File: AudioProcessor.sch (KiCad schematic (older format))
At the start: 57 parts, among them J601 Conn_01x03_Female, J602 Conn_02x01, J603 Conn_02x06_Odd_Even, Q501 2N7002, U502 BK8000L, U503 TDA7719, U504 AP2553AW6-7, U505 JW5026

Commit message: Bauteilwerte verändert
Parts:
- R513, R520, R521: value 10K -> 100K
- R514: value 100R -> 1K
- R523, R524: value 47R -> 100R
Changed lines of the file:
@@
 P 1150 6050
 F 0 "R513" H 1000 6000 50  0000 C CNN
-F 1 "10K" H 950 6100 50  0000 C CNN
+F 1 "100K" H 950 6100 50  0000 C CNN
 F 2 "Resistor_SMD:R_0603_1608Metric_Pad1.05x0.95mm_HandSolder" H 1150 6050 50  0001 C CNN
 F 3 "~" H 1150 6050 50  0001 C CNN
@@
 P 1550 5950
 F 0 "R514" V 1450 5800 50  0000 C CNN
-F 1 "100R" V 1450 6100 50  0000 C CNN
+F 1 "1K" V 1450 6100 50  0000 C CNN
 F 2 "Resistor_SMD:R_0603_1608Metric_Pad1.05x0.95mm_HandSolder" H 1550 5950 50  0001 C CNN
 F 3 "~" H 1550 5950 50  0001 C CNN
@@
 P 7450 3050
 F 0 "R523" V 7350 2900 50  0000 C CNN
-F 1 "47R" V 7350 3200 50  0000 C CNN
+F 1 "100R" V 7350 3200 50  0000 C CNN
 F 2 "Resistor_SMD:R_0603_1608Metric_Pad1.05x0.95mm_HandSolder" H 7450 3050 50  0001 C CNN
 F 3 "~" H 7450 3050 50  0001 C CNN
@@
 P 7450 3200
 F 0 "R524" V 7350 3050 50  0000 C CNN
-F 1 "47R" V 7350 3350 50  0000 C CNN
+F 1 "100R" V 7350 3350 50  0000 C CNN
 F 2 "Resistor_SMD:R_0603_1608Metric_Pad1.05x0.95mm_HandSolder" H 7450 3200 50  0001 C CNN
 F 3 "~" H 7450 3200 50  0001 C CNN
@@
 P 2300 4400
 F 0 "R521" V 2500 4400 50  0000 C CNN
-F 1 "10K" V 2400 4400 50  0000 C CNN
+F 1 "100K" V 2400 4400 50  0000 C CNN
 F 2 "Resistor_SMD:R_0603_1608Metric_Pad1.05x0.95mm_HandSolder" H 2300 4400 50  0001 C CNN
 F 3 "~" H 2300 4400 50  0001 C CNN
@@
 P 1300 4200
 F 0 "R520" H 1150 4250 50  0000 C CNN
-F 1 "10K" H 1150 4150 50  0000 C CNN
+F 1 "100K" H 1150 4150 50  0000 C CNN
 F 2 "Resistor_SMD:R_0603_1608Metric_Pad1.05x0.95mm_HandSolder" H 1300 4200 50  0001 C CNN
 F 3 "~" H 1300 4200 50  0001 C CNN

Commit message: Bereit zur Bestellung
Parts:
- removed C509, C536: 10u, Capacitor_THT:CP_Radial_D4.0mm_P2.00mm, symbol Device:CP1_Small
- removed TP502: TestPoint, TestPoint:TestPoint_Pad_1.0x1.0mm, symbol Connector:TestPoint
- added C509, C536: 10u, Capacitor_SMD:C_1206_3216Metric_Pad1.42x1.75mm_HandSolder, symbol Device:C_Small
- added R20: DNP, Resistor_SMD:R_0603_1608Metric_Pad1.05x0.95mm_HandSolder, symbol Device:R_Small
- C503, C508, C542: footprint Capacitor_THT:CP_Radial_D4.0mm_P2.00mm -> Capacitor_SMD:C_1206_3216Metric_Pad1.42x1.75mm_HandSolder; symbol Device:CP1_Small -> Device:C_Small
- U502: symbol MukkeBox-rescue:BK8000L-RF_Bluetooth -> MukkeBox-rescue:BK8000L-RF_Bluetooth-MukkeBox-rescue
- U503: symbol MukkeBox-rescue:TDA7719-MySymbols -> MukkeBox-rescue:TDA7719-MySymbols-MukkeBox-rescue
- U504: symbol MukkeBox-rescue:AP2553-MySymbols -> MukkeBox-rescue:AP2553-MySymbols-MukkeBox-rescue
- U505: symbol MukkeBox-rescue:TPS560430-Regulator_Switching -> MukkeBox-rescue:TPS560430-Regulator_Switching-MukkeBox-rescue
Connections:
- net labels added: LEVELMETER, TO_SUB
- wire segments 183 -> 182
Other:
- moved on the sheet: R617
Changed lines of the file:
@@
 EESchema Schematic File Version 4
-LIBS:MukkeBox-cache
-EELAYER 26 0
+EELAYER 30 0
 EELAYER END
 $Descr A4 11693 8268
@@
 Wire Wire Line
 	5000 4100 4700 4100
-Text GLabel 9900 3700 2    50   Output ~ 0
+Text GLabel 9900 3400 2    50   Output ~ 0
 TO_SPEAKER_L
-Text GLabel 9900 4100 2    50   Output ~ 0
+Text GLabel 9900 4000 2    50   Output ~ 0
 TO_SPEAKER_R
 Text Notes 5700 4950 0    50   ~ 0
@@
 	3350 3250 3350 3100
 Wire Wire Line
-	8250 4000 8150 4000
+	8250 4000 8200 4000
 Wire Wire Line
 	8150 3700 8250 3700
-Wire Wire Line
-	9900 3700 9400 3700
-Wire Wire Line
-	9900 4100 9400 4100
 $Comp
 L Device:R_Small R615
@@
 	8950 3900 8750 3900
 Wire Wire Line
-	9150 3800 9200 3800
-Wire Wire Line
-	9200 3800 9200 3850
-Wire Wire Line
-	9200 3900 9150 3900
-Wire Wire Line
-	9200 3850 9400 3850
-Wire Wire Line
-	9400 3850 9400 3700
-Connection ~ 9200 3850
-Wire Wire Line
-	9200 3850 9200 3900
-Wire Wire Line
-	9400 4000 9400 4100
-Wire Wire Line
-	8250 3900 8150 3900
-Wire Wire Line
-	8150 3900 8150 3950
-Wire Wire Line
-	8250 3800 8150 3800
-Wire Wire Line
-	8150 3800 8150 3750
-Wire Wire Line
 	4950 3000 3650 3000
 Connection ~ 3650 3000
@@
 L Device:R_Small R617
 U 1 1 5E9FC4EB
-P 9650 3850
-F 0 "R617" V 9750 3800 50  0000 L CNN
-F 1 "DNP" V 9850 3800 50  0000 L CNN
-F 2 "Resistor_SMD:R_0603_1608Metric_Pad1.05x0.95mm_HandSolder" H 9650 3850 50  0001 C CNN
-F 3 "~" H 9650 3850 50  0001 C CNN
-	1    9650 3850
-	0    1    1    0
-$EndComp
-Wire Wire Line
-	9550 3850 9400 3850
-Connection ~ 9400 3850
+P 10000 3500
+F 0 "R617" V 10050 3250 50  0000 L CNN
+F 1 "DNP" V 10150 3250 50  0000 L CNN
+F 2 "Resistor_SMD:R_0603_1608Metric_Pad1.05x0.95mm_HandSolder" H 10000 3500 50  0001 C CNN
+F 3 "~" H 10000 3500 50  0001 C CNN
+	1    10000 3500
+	0    1    1    0
+$EndComp
 $Comp
 L power:GNDA #PWR0185
 U 1 1 5E9FF2F0
-P 9750 3850
-F 0 "#PWR0185" H 9750 3600 50  0001 C CNN
-F 1 "GNDA" V 9700 3650 50  0000 C CNN
-F 2 "" H 9750 3850 50  0001 C CNN
-F 3 "" H 9750 3850 50  0001 C CNN
-	1    9750 3850
+P 10100 3500
+F 0 "#PWR0185" H 10100 3250 50  0001 C CNN
+F 1 "GNDA" V 10050 3300 50  0000 C CNN
+F 2 "" H 10100 3500 50  0001 C CNN
+F 3 "" H 10100 3500 50  0001 C CNN
+	1    10100 3500
 	0    -1   -1   0
 $EndComp
@@
 $EndComp
 Wire Wire Line
-	9150 3700 9400 3700
-Connection ~ 9400 3700
-Wire Wire Line
 	8950 3700 8750 3700
 Wire Wire Line
@@
 	8950 4100 8750 4100
 Wire Wire Line
-	9150 4000 9400 4000
-Wire Wire Line
 	9150 4100 9400 4100
-Connection ~ 9400 4100
 Wire Wire Line
 	7000 3100 7150 3100
@@
 	7550 1100 7700 1100
 $Comp
-L MukkeBox-rescue:TDA7719-MySymbols U503
+L MukkeBox-rescue:TDA7719-MySymbols-MukkeBox-rescue U503
 U 1 1 5EF6B5F5
 P 6350 3700
@@
 NoConn ~ 5750 3700
 $Comp
-L Device:CP1_Small C?
+L Device:C_Small C?
 U 1 1 5F02DF45
 P 6450 1350
@@
 F 0 "C508" H 6541 1396 50  0000 L CNN
 F 1 "10u" H 6541 1305 50  0000 L CNN
-F 2 "Capacitor_THT:CP_Radial_D4.0mm_P2.00mm" H 6450 1350 50  0001 C CNN
+F 2 "Capacitor_SMD:C_1206_3216Metric_Pad1.42x1.75mm_HandSolder" H 6450 1350 50  0001 C CNN
 F 3 "~" H 6450 1350 50  0001 C CNN
 	1    6450 1350
 	1    0    0    -1
 $EndComp
-$Comp
-L Device:CP1_Small C?
-U 1 1 5F03288E
-P 5650 4450
-AR Path="/5E73BB4A/5F03288E" Ref="C?"  Part="1"
-AR Path="/5EA6895E/5F03288E" Ref="C509"  Part="1"
-F 0 "C509" H 5741 4496 50  0000 L CNN
-F 1 "10u" H 5741 4405 50  0000 L CNN
-F 2 "Capacitor_THT:CP_Radial_D4.0mm_P2.00mm" H 5650 4450 50  0001 C CNN
-F 3 "~" H 5650 4450 50  0001 C CNN
-	1    5650 4450
-	1    0    0    -1
-$EndComp
 Wire Wire Line
 	5750 4200 5650 4200
 Wire Wire Line
 	5650 4200 5650 4350
-$Comp
-L Device:CP1_Small C?
-U 1 1 5F0361D0
-P 7450 3500
-AR Path="/5E73BB4A/5F0361D0" Ref="C?"  Part="1"
-AR Path="/5EA6895E/5F0361D0" Ref="C536"  Part="1"
-F 0 "C536" V 7500 3550 50  0000 L CNN
-F 1 "10u" V 7500 3300 50  0000 L CNN
-F 2 "Capacitor_THT:CP_Radial_D4.0mm_P2.00mm" H 7450 3500 50  0001 C CNN
-F 3 "~" H 7450 3500 50  0001 C CNN
-	1    7450 3500
-	0    -1   -1   0
-$EndComp
 Wire Wire Line
 	7700 3500 7550 3500
@@
 	1    0    0    -1
 $EndComp
-$Comp
-L Connector:TestPoint TP502
-U 1 1 5F04C2E9
-P 7700 2700
-F 0 "TP502" H 7758 2820 50  0000 L CNN
-F 1 "TestPoint" H 7758 2729 50  0000 L CNN
-F 2 "TestPoint:TestPoint_Pad_1.0x1.0mm" H 7900 2700 50  0001 C CNN
-F 3 "~" H 7900 2700 50  0001 C CNN
-	1    7700 2700
-	1    0    0    -1
-$EndComp
 Wire Wire Line
 	7000 3400 8400 3400
@@
 Wire Wire Line
 	7000 3000 7700 3000
-Wire Wire Line
-	7700 3000 7700 2700
 $Comp
 L Connector:TestPoint TP503
@@
 Wire Wire Line
 	7550 3750 8150 3750
-Connection ~ 8150 3750
 Wire Wire Line
 	8150 3750 8150 3700
@@
 Wire Wire Line
 	7250 4000 7350 4000
-Wire Wire Line
-	8150 3950 7700 3950
-Wire Wire Line
-	7700 3950 7700 4000
-Wire Wire Line
-	7700 4000 7550 4000
-Connection ~ 8150 3950
-Wire Wire Line
-	8150 3950 8150 4000
 Wire Wire Line
 	7700 4100 7700 4250
@@
 	2700 6050 2950 6050
 $Comp
-L MukkeBox-rescue:BK8000L-RF_Bluetooth U502
+L MukkeBox-rescue:BK8000L-RF_Bluetooth-MukkeBox-rescue U502
 U 1 1 5ECB4DA7
 P 3350 5800
@@
 $EndComp
 $Comp
-L Device:CP1_Small C?
+L Device:C_Small C?
 U 1 1 5FE1C5A0
 P 5300 5500
@@
 F 0 "C542" H 5391 5546 50  0000 L CNN
 F 1 "10u" H 5391 5455 50  0000 L CNN
-F 2 "Capacitor_THT:CP_Radial_D4.0mm_P2.00mm" H 5300 5500 50  0001 C CNN
+F 2 "Capacitor_SMD:C_1206_3216Metric_Pad1.42x1.75mm_HandSolder" H 5300 5500 50  0001 C CNN
 F 3 "~" H 5300 5500 50  0001 C CNN
 	1    5300 5500
@@
 $EndComp
 $Comp
-L MukkeBox-rescue:AP2553-MySymbols U504
+L MukkeBox-rescue:AP2553-MySymbols-MukkeBox-rescue U504
 U 1 1 5ED20D23
 P 1700 3900
@@
 	5100 5150 5100 5350
 $Comp
-L MukkeBox-rescue:TPS560430-Regulator_Switching U?
+L MukkeBox-rescue:TPS560430-Regulator_Switching-MukkeBox-rescue U?
 U 1 1 5EDC547A
 P 4700 1050
@@
 	6450 1450 6450 1600
 $Comp
-L Device:CP1_Small C?
+L Device:C_Small C?
 U 1 1 5EDC54C5
 P 2650 1150
@@
 F 0 "C503" H 2741 1196 50  0000 L CNN
 F 1 "10u" H 2741 1105 50  0000 L CNN
-F 2 "Capacitor_THT:CP_Radial_D4.0mm_P2.00mm" H 2650 1150 50  0001 C CNN
+F 2 "Capacitor_SMD:C_1206_3216Metric_Pad1.42x1.75mm_HandSolder" H 2650 1150 50  0001 C CNN
 F 3 "~" H 2650 1150 50  0001 C CNN
 	1    2650 1150
@@
 Wire Wire Line
 	4400 6550 4100 6550
+Text GLabel 9900 4200 2    50   Output ~ 0
+TO_SUB
+Wire Wire Line
+	9150 4000 9400 4000
+Wire Wire Line
+	9900 4200 9400 4200
+Wire Wire Line
+	8250 3900 8150 3900
+Wire Wire Line
+	8150 3900 8150 3750
+Connection ~ 8150 3750
+Wire Wire Line
+	8250 3800 8200 3800
+Wire Wire Line
+	8200 3800 8200 4000
+Connection ~ 8200 4000
+Wire Wire Line
+	7550 4000 8200 4000
+Wire Wire Line
+	9150 3700 9400 3700
+Wire Wire Line
+	9150 3900 9400 3900
+Wire Wire Line
+	9400 3900 9400 4000
+Connection ~ 9400 4000
+Wire Wire Line
+	9400 4000 9900 4000
+Wire Wire Line
+	9150 3800 9400 3800
+Wire Wire Line
+	9400 3800 9400 3700
+Connection ~ 9400 3700
+Wire Wire Line
+	9900 3400 9400 3400
+Wire Wire Line
+	9400 3400 9400 3500
+Wire Wire Line
+	9900 3500 9400 3500
+Connection ~ 9400 3500
+Wire Wire Line
+	9400 3500 9400 3700
+$Comp
+L Device:R_Small R20
+U 1 1 60022DD1
+P 10000 3900
+F 0 "R20" V 9850 3650 50  0000 L CNN
+F 1 "DNP" V 9950 3650 50  0000 L CNN
+F 2 "Resistor_SMD:R_0603_1608Metric_Pad1.05x0.95mm_HandSolder" H 10000 3900 50  0001 C CNN
+F 3 "~" H 10000 3900 50  0001 C CNN
+	1    10000 3900
+	0    1    1    0
+$EndComp
+$Comp
+L power:GNDA #PWR027
+U 1 1 60022DD7
+P 10100 3900
+F 0 "#PWR027" H 10100 3650 50  0001 C CNN
+F 1 "GNDA" V 10150 3700 50  0000 C CNN
+F 2 "" H 10100 3900 50  0001 C CNN
+F 3 "" H 10100 3900 50  0001 C CNN
+	1    10100 3900
+	0    -1   -1   0
+$EndComp
+Wire Wire Line
+	9900 3900 9400 3900
+Connection ~ 9400 3900
+Text GLabel 7900 2250 2    50   Output ~ 0
+LEVELMETER
+Wire Wire Line
+	7900 2250 7700 2250
+Wire Wire Line
+	7700 2250 7700 3000
+$Comp
+L Device:C_Small C509
+U 1 1 5F691ED3
+P 5650 4450
+F 0 "C509" H 5450 4400 50  0000 L CNN
+F 1 "10u" H 5450 4500 50  0000 L CNN
+F 2 "Capacitor_SMD:C_1206_3216Metric_Pad1.42x1.75mm_HandSolder" H 5650 4450 50  0001 C CNN
+F 3 "https://www.mouser.de/datasheet/2/212/KEM_F3101_R82-1103738.pdf" H 5650 4450 50  0001 C CNN
+	1    5650 4450
+	-1   0    0    1
+$EndComp
+$Comp
+L Device:C_Small C536
+U 1 1 5F694351
+P 7450 3500
+F 0 "C536" V 7500 3250 50  0000 L CNN
+F 1 "10u" V 7500 3600 50  0000 L CNN
+F 2 "Capacitor_SMD:C_1206_3216Metric_Pad1.42x1.75mm_HandSolder" H 7450 3500 50  0001 C CNN
+F 3 "https://www.mouser.de/datasheet/2/212/KEM_F3101_R82-1103738.pdf" H 7450 3500 50  0001 C CNN
+	1    7450 3500
+	0    -1   -1   0
+$EndComp
 $EndSCHEMATC

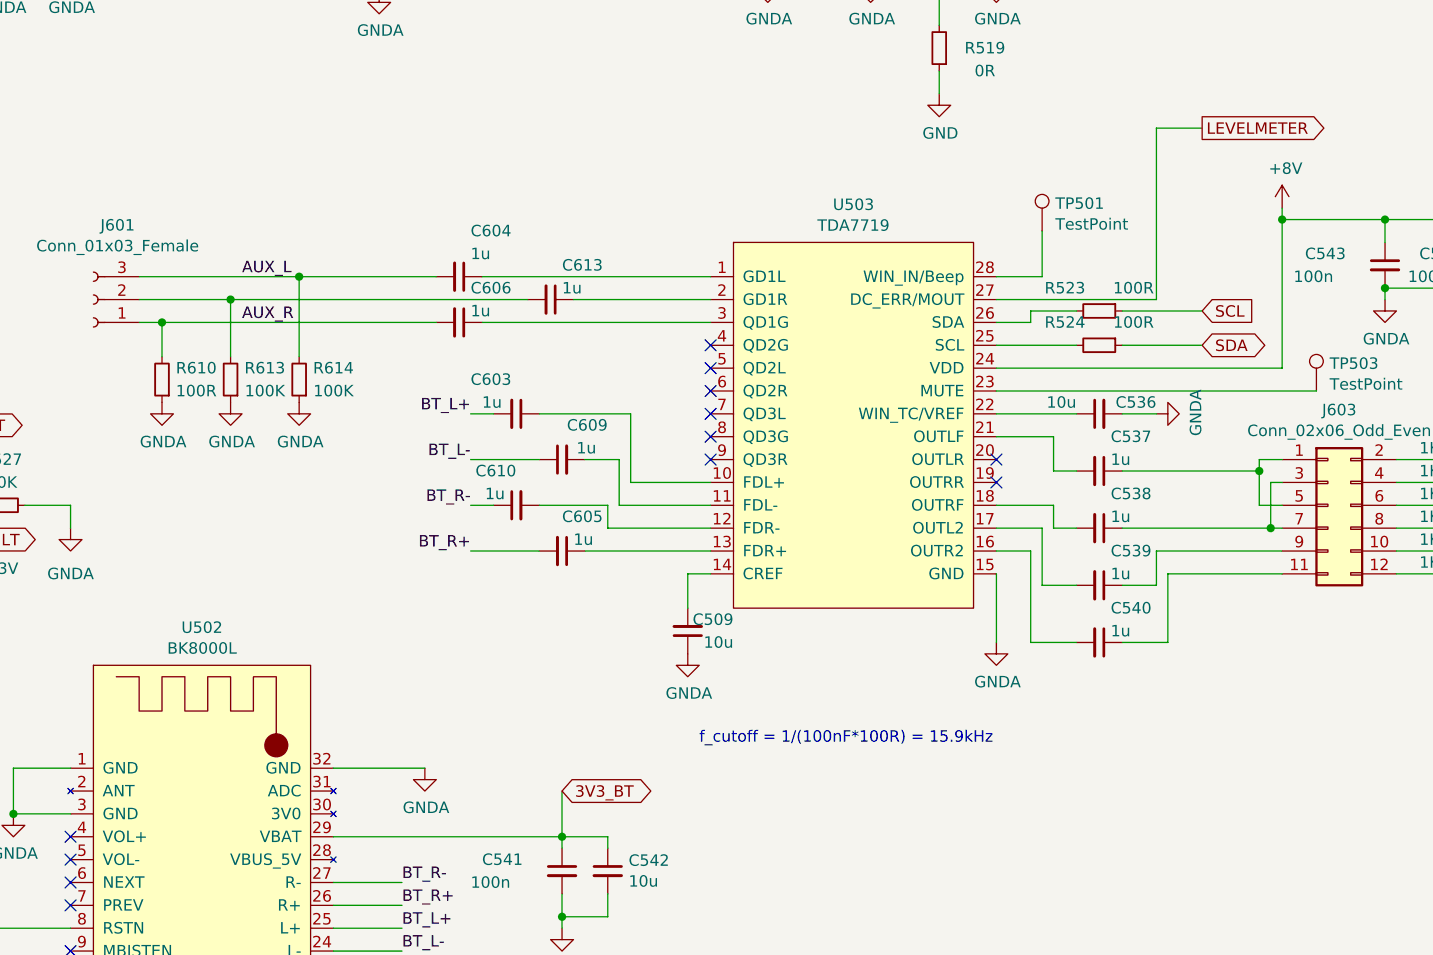
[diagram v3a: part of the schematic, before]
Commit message: Footprints parallel zu Folienkondensatoren hinzugefügt; Bestellung ist abgeschickt!
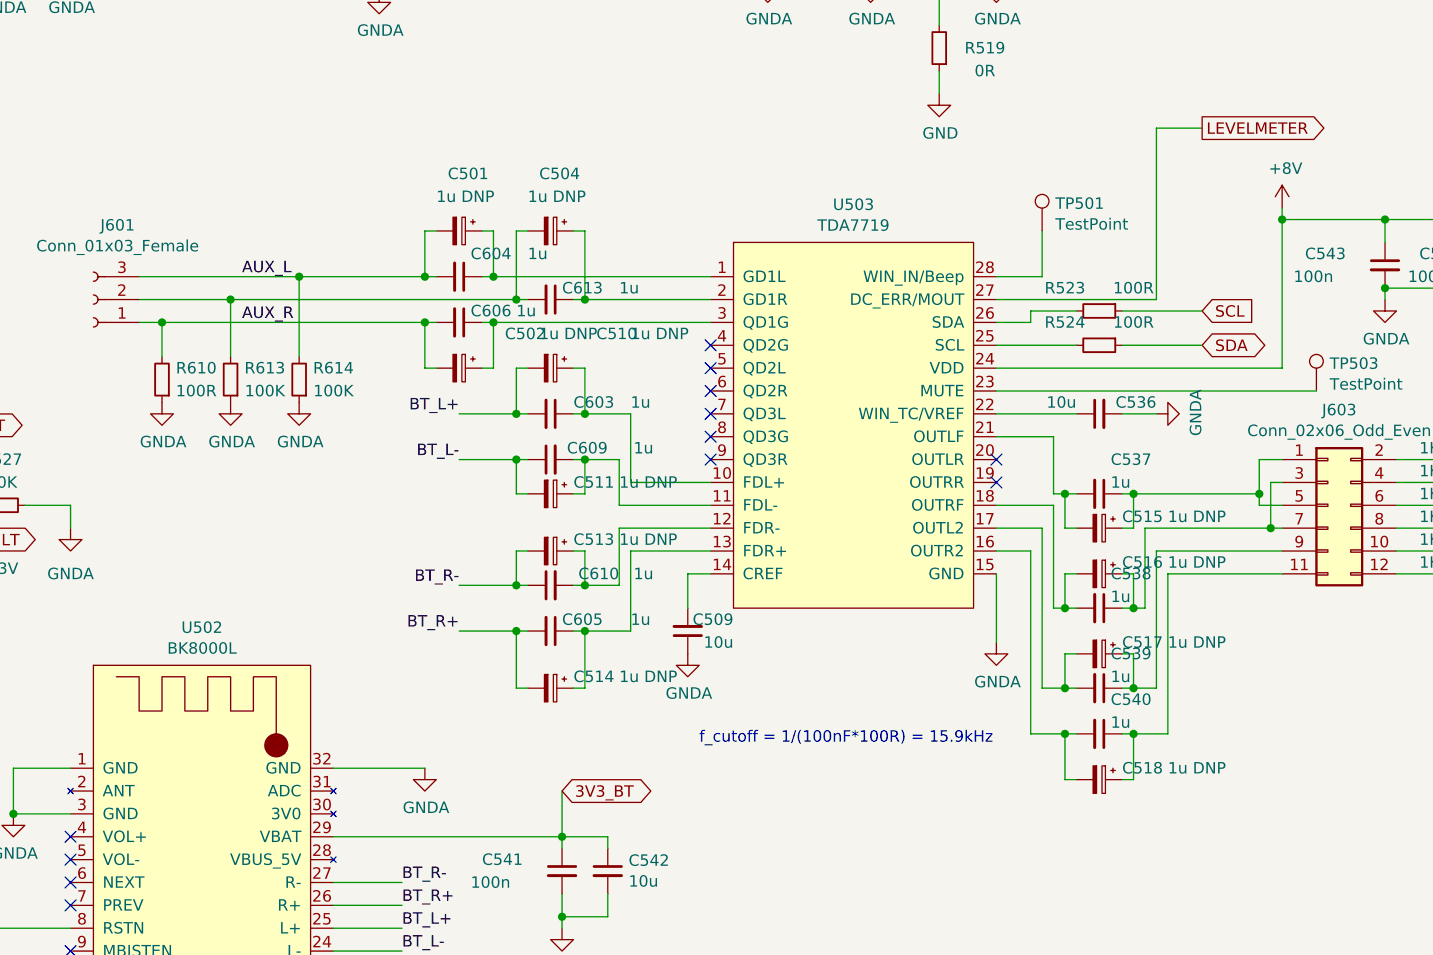
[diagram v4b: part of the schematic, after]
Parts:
- added C501, C502, C504, C510, C511, C513, C514, C515, C516, C517, C518: 1u DNP, Capacitor_Tantalum_SMD:CP_EIA-3216-18_Kemet-A, symbol Device:CP_Small
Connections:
- net AUX_L: now also C501.2
- net AUX_R: now also C502.2
- net BT_L+: now also C510.2
- net BT_L-: now also C511.2
- net BT_R+: now also C514.2
- net BT_R-: now also C513.2
- net at C613.2, J601.2 (Pin_2), R613.2: now also C504.2
- net at C603.1, U503.10 (FDL+): now also C510.1
- net at C605.1, U503.13 (FDR+): now also C514.1
- net at C604.1, U503.1 (GD1L): now also C501.1
- net at C606.1, U503.3 (QD1G): now also C502.1
- net at C609.2, U503.11 (FDL-): now also C511.1
- net at C610.2, U503.12 (FDR-): now also C513.1
- net at C613.1, U503.2 (GD1R): now also C504.1
- net at C540.2, U503.16 (OUTR2): now also C518.2
- net at C539.2, U503.17 (OUTL2): now also C517.2
- net at C538.2, U503.18 (OUTRF): now also C516.2
- net at C537.2, U503.21 (OUTLF): now also C515.2
- net at C537.1, J603.1 (Pin_1), J603.5 (Pin_5): now also C515.1
- net at C540.1, J603.11 (Pin_11): now also C518.1
- net at C538.1, J603.3 (Pin_3), J603.7 (Pin_7): now also C516.1
- net at C539.1, J603.9 (Pin_9): now also C517.1
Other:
- moved on the sheet: C537, C538, C539, C540, C603, C605, C609, C610
